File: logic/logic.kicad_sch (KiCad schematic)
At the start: 22 parts, among them J1 DIN41612_02x32_AC, U1 TPIC6595, U2 TPIC6595, U3 TPIC6595, U4 TPIC6595, U5 TPIC6595, U6 TPIC6595, U7 TPIC6595, U8 TPIC6595, U9 74HC14

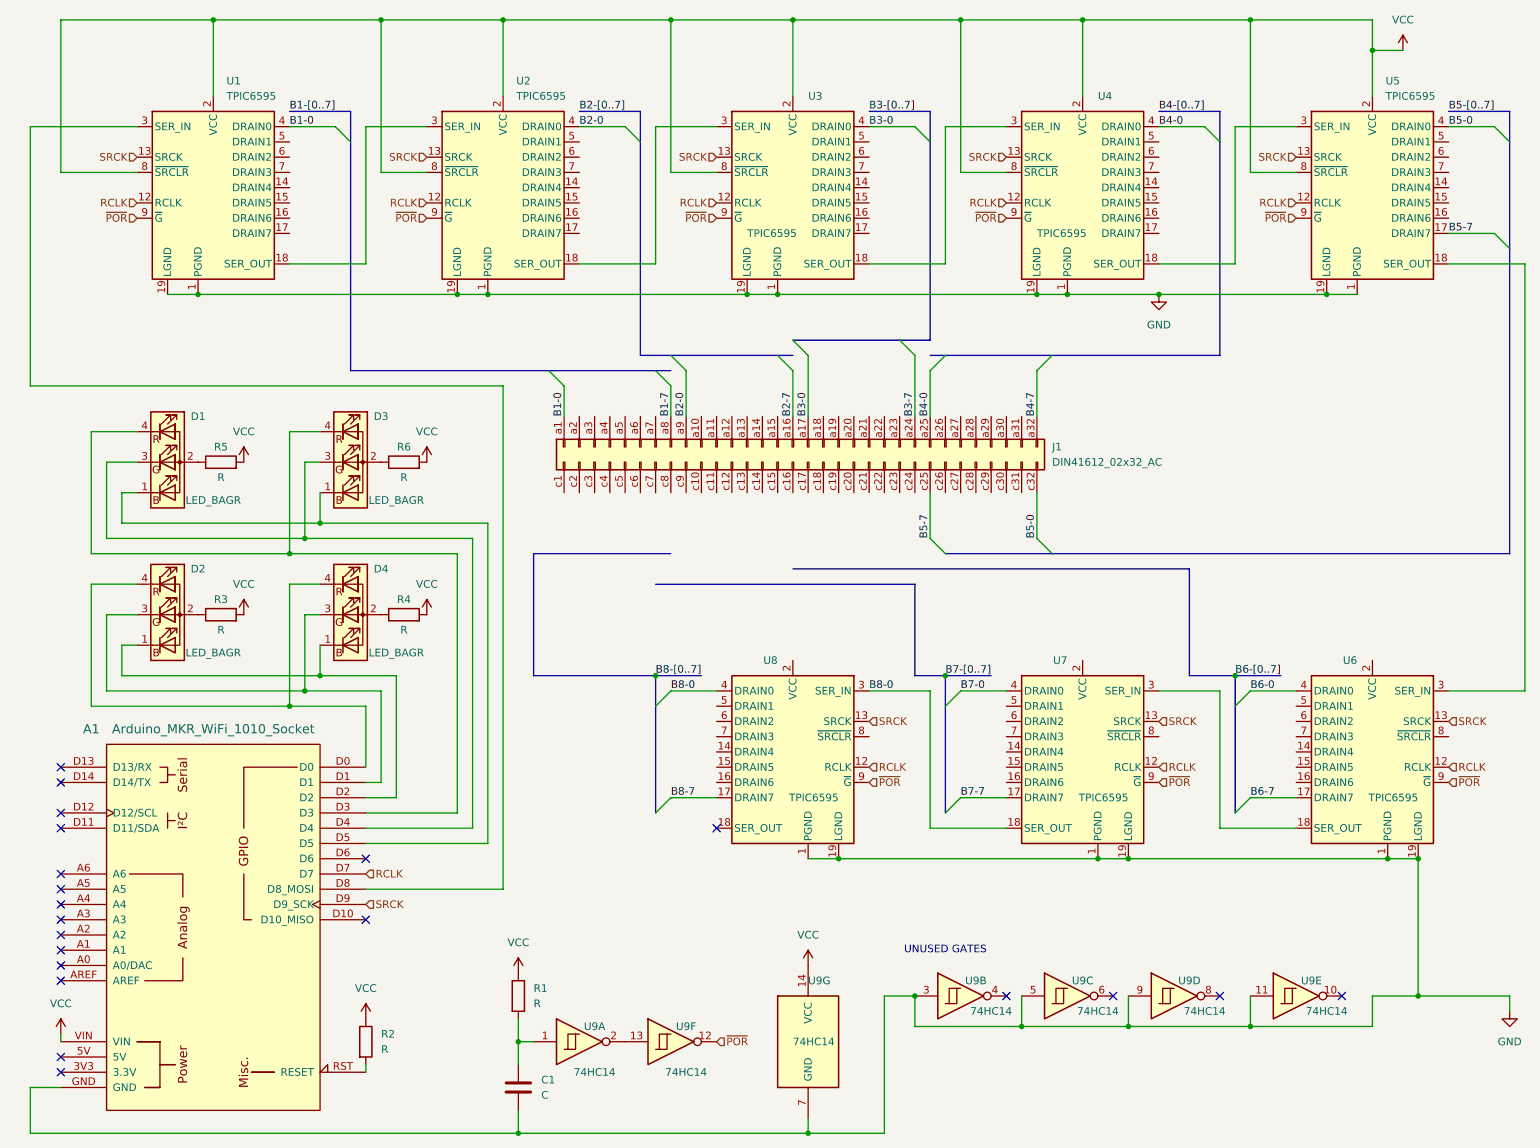
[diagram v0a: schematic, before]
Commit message: Commit obsolete version before major revision
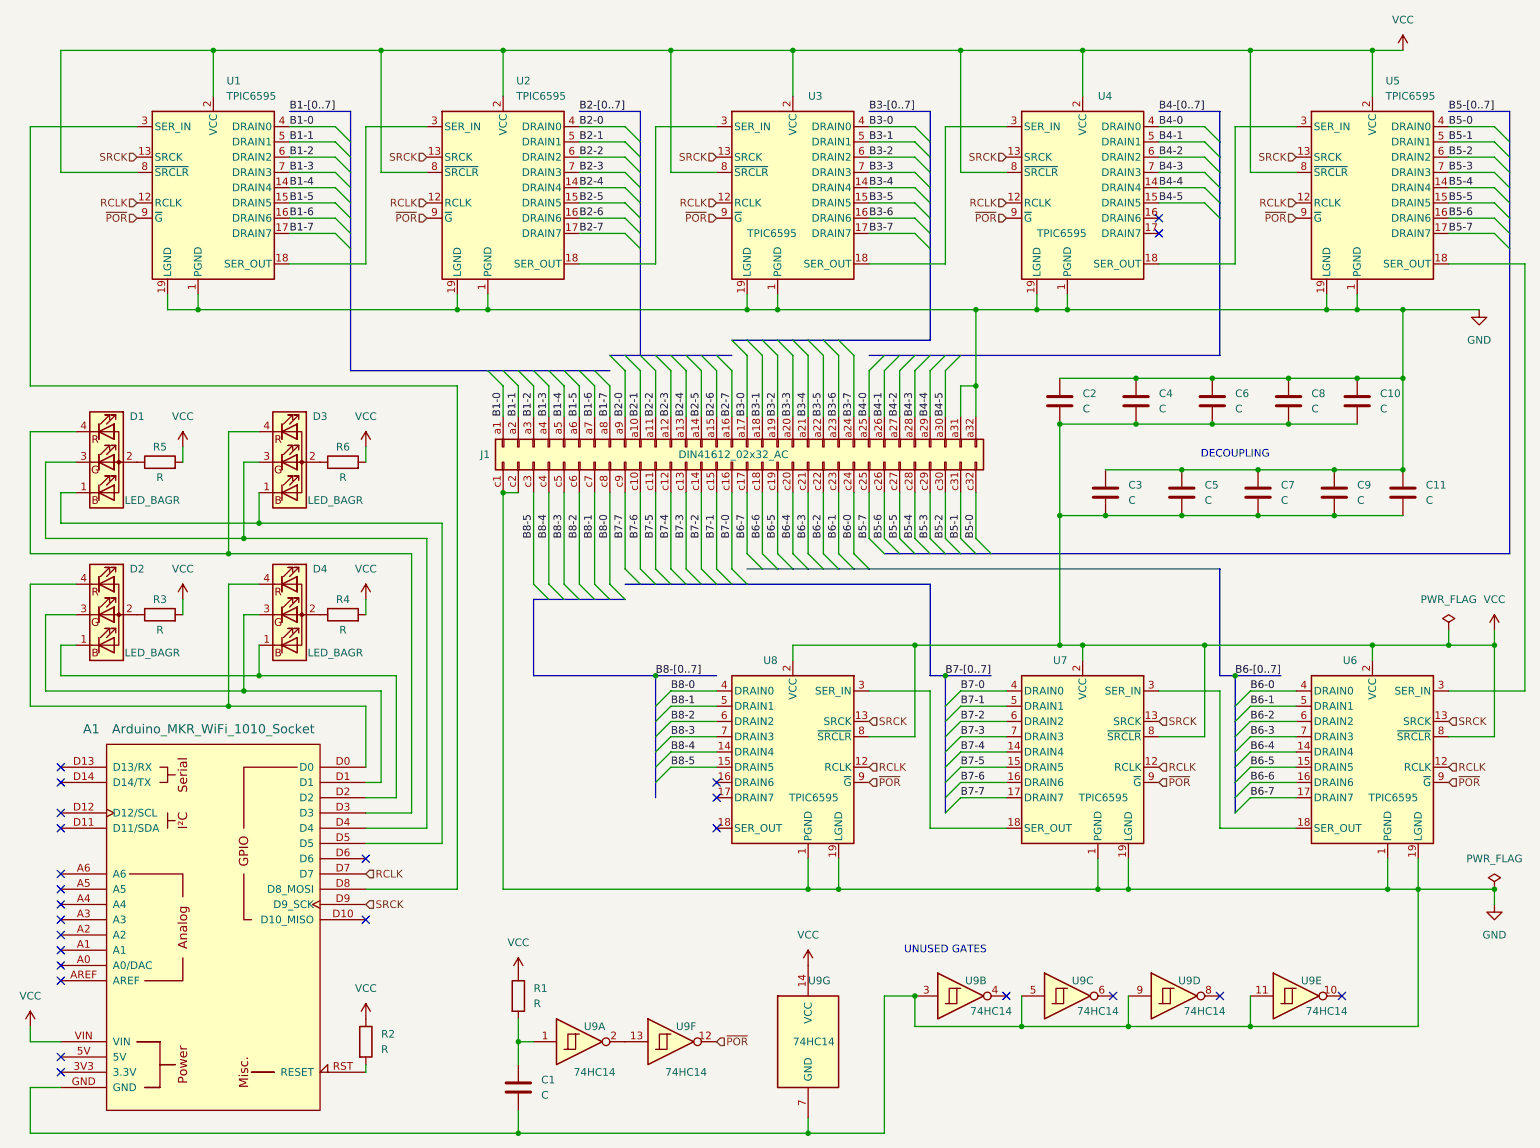
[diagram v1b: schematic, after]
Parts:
- added C10, C11, C2, C3, C4, C5, C6, C7, C8, C9: C, symbol Device:C
- J1: footprint (none) -> Connector_DIN:DIN41612_R_2x32_Male_Vertical_THT
- U1: footprint (none) -> Package_DIP:DIP-20_W7.62mm_Socket
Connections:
- net B4-7 is gone; now on net GND: J1.a32 (Pin_a32)
- net B1-7: now also U1.17 (DRAIN7)
- net B2-7: now also U2.17 (DRAIN7)
- net B3-7: now also U3.17 (DRAIN7)
- net B6-0: now also J1.c24 (Pin_c24)
- net B6-7: now also J1.c17 (Pin_c17)
- net B7-0: now also J1.c16 (Pin_c16)
- net B7-7: now also J1.c9 (Pin_c9)
- net B8-0: now also J1.c8 (Pin_c8); no longer U7.18 (SER_OUT), U8.3 (SER_IN)
- net GND: now also J1.a31 (Pin_a31), J1.c1 (Pin_c1), J1.c2 (Pin_c2), C10.1, C11.1, C2.1, C3.1, C4.1, C5.1, C6.1, C7.1, C8.1, C9.1
- net VCC: now also U6.2 (VCC), U6.8 (~{SRCLR}), U7.2 (VCC), U7.8 (~{SRCLR}), U8.2 (VCC), U8.8 (~{SRCLR}), C10.2, C11.2, C2.2, C3.2, C4.2, C5.2, C6.2, C7.2, C8.2, C9.2
- net B3-4: now reaches U3.14 (DRAIN4)
- net B3-4: now also J1.a21 (Pin_a21)
- net B3-5: now reaches U3.15 (DRAIN5)
- net B3-5: now also J1.a22 (Pin_a22)
- net B3-6: now reaches U3.16 (DRAIN6)
- net B3-6: now also J1.a23 (Pin_a23)
- net B3-1: now reaches U3.5 (DRAIN1)
- net B3-1: now also J1.a18 (Pin_a18)
- net B3-2: now reaches U3.6 (DRAIN2)
- net B3-2: now also J1.a19 (Pin_a19)
- net B3-3: now reaches U3.7 (DRAIN3)
- net B3-3: now also J1.a20 (Pin_a20)
- net B2-4: now reaches U2.14 (DRAIN4)
- net B2-4: now also J1.a13 (Pin_a13)
- net B2-5: now reaches U2.15 (DRAIN5)
- net B2-5: now also J1.a14 (Pin_a14)
- net B2-6: now reaches U2.16 (DRAIN6)
- net B2-6: now also J1.a15 (Pin_a15)
- net B2-1: now reaches U2.5 (DRAIN1)
- net B2-1: now also J1.a10 (Pin_a10)
- net B2-2: now reaches U2.6 (DRAIN2)
- net B2-2: now also J1.a11 (Pin_a11)
- net B2-3: now reaches U2.7 (DRAIN3)
- net B2-3: now also J1.a12 (Pin_a12)
- net B1-4: now reaches U1.14 (DRAIN4)
- net B1-4: now also J1.a5 (Pin_a5)
- net B1-5: now reaches U1.15 (DRAIN5)
- net B1-5: now also J1.a6 (Pin_a6)
- net B1-6: now reaches U1.16 (DRAIN6)
- net B1-6: now also J1.a7 (Pin_a7)
- net B1-1: now reaches U1.5 (DRAIN1)
- net B1-1: now also J1.a2 (Pin_a2)
- net B1-2: now reaches U1.6 (DRAIN2)
- net B1-2: now also J1.a3 (Pin_a3)
- net B1-3: now reaches U1.7 (DRAIN3)
- net B1-3: now also J1.a4 (Pin_a4)
- net B4-1: now reaches J1.a26 (Pin_a26)
- net B4-1: now also U4.5 (DRAIN1)
- net B4-2: now reaches J1.a27 (Pin_a27)
- net B4-2: now also U4.6 (DRAIN2)
- net B4-3: now reaches J1.a28 (Pin_a28)
- net B4-3: now also U4.7 (DRAIN3)
- net B4-4: now reaches J1.a29 (Pin_a29)
- net B4-4: now also U4.14 (DRAIN4)
- net B4-5: now reaches J1.a30 (Pin_a30)
- net B4-5: now also U4.15 (DRAIN5)
- net B7-6: now reaches J1.c10 (Pin_c10)
- net B7-6: now also U7.16 (DRAIN6)
- net B7-5: now reaches J1.c11 (Pin_c11)
- net B7-5: now also U7.15 (DRAIN5)
- net B7-4: now reaches J1.c12 (Pin_c12)
- net B7-4: now also U7.14 (DRAIN4)
- net B7-3: now reaches J1.c13 (Pin_c13)
- net B7-3: now also U7.7 (DRAIN3)
- net B7-2: now reaches J1.c14 (Pin_c14)
- net B7-2: now also U7.6 (DRAIN2)
- net B7-1: now reaches J1.c15 (Pin_c15)
- net B7-1: now also U7.5 (DRAIN1)
- net B6-6: now reaches J1.c18 (Pin_c18)
- net B6-6: now also U6.16 (DRAIN6)
- net B6-5: now reaches J1.c19 (Pin_c19)
- net B6-5: now also U6.15 (DRAIN5)
- net B6-4: now reaches J1.c20 (Pin_c20)
- net B6-4: now also U6.14 (DRAIN4)
- net B6-3: now reaches J1.c21 (Pin_c21)
- net B6-3: now also U6.7 (DRAIN3)
- net B6-2: now reaches J1.c22 (Pin_c22)
- net B6-2: now also U6.6 (DRAIN2)
- net B6-1: now reaches J1.c23 (Pin_c23)
- net B6-1: now also U6.5 (DRAIN1)
- net B5-6: now reaches J1.c26 (Pin_c26)
- net B5-6: now also U5.16 (DRAIN6)
- net B5-5: now reaches J1.c27 (Pin_c27)
- net B5-5: now also U5.15 (DRAIN5)
- net B5-4: now reaches J1.c28 (Pin_c28)
- net B5-4: now also U5.14 (DRAIN4)
- net B5-3: now reaches J1.c29 (Pin_c29)
- net B5-3: now also U5.7 (DRAIN3)
- net B8-5: now reaches J1.c3 (Pin_c3)
- net B8-5: now also U8.15 (DRAIN5)
- net B5-2: now reaches J1.c30 (Pin_c30)
- net B5-2: now also U5.6 (DRAIN2)
- net B5-1: now reaches J1.c31 (Pin_c31)
- net B5-1: now also U5.5 (DRAIN1)
- net B8-4: now reaches J1.c4 (Pin_c4)
- net B8-4: now also U8.14 (DRAIN4)
- net B8-3: now reaches J1.c5 (Pin_c5)
- net B8-3: now also U8.7 (DRAIN3)
- net B8-2: now reaches J1.c6 (Pin_c6)
- net B8-2: now also U8.6 (DRAIN2)
- net B8-1: now reaches J1.c7 (Pin_c7)
- net B8-1: now also U8.5 (DRAIN1)
- net B8-7: no longer names the net of U8.17 (DRAIN7)
- new net: U7.18 (SER_OUT), U8.3 (SER_IN)
- no-connect marks 21 -> 25
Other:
- note added: "DECOUPLING"
- moved on the sheet: D1, D2, D3, D4, J1, R3, R4, R5, R6

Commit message: Change to new 96-pin DIN-41612 schematic symbol in custom library
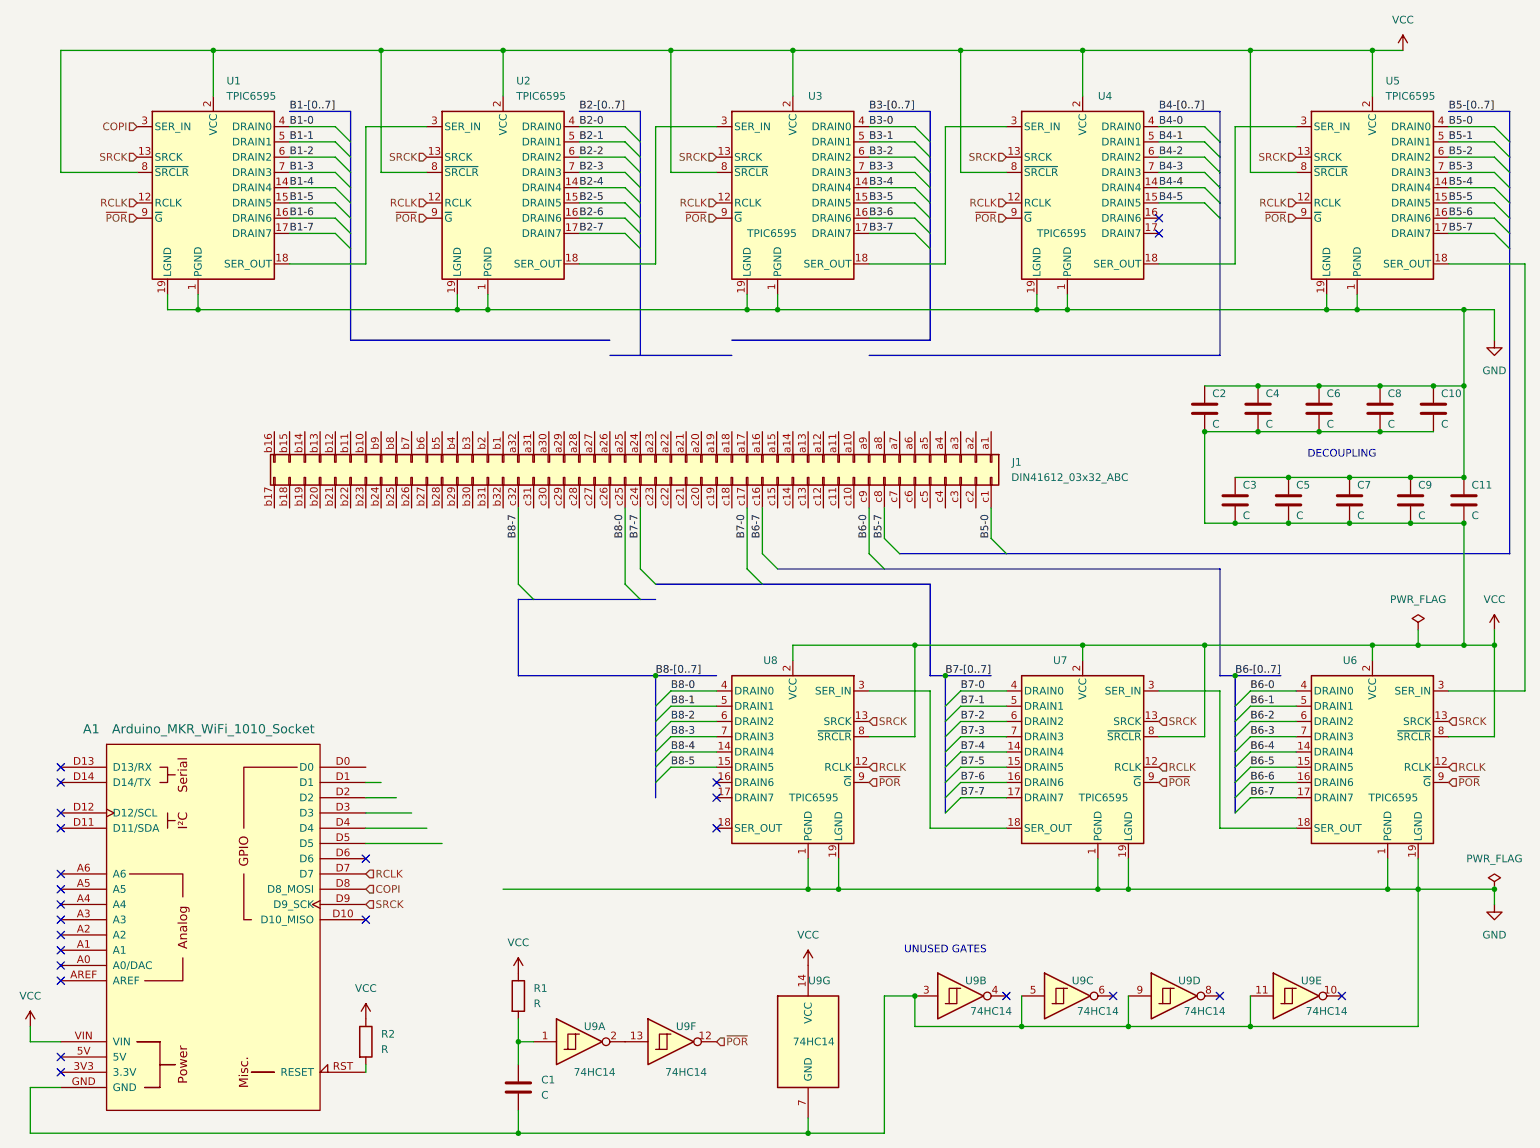
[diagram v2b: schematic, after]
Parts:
- removed D1, D2, D3, D4: LED_BAGR, symbol Device:LED_BAGR
- removed J1: DIN41612_02x32_AC, Connector_DIN:DIN41612_R_2x32_Male_Vertical_THT, symbol Connector:DIN41612_02x32_AC
- removed R3, R4, R5, R6: R, symbol Device:R
- added J1: DIN41612_03x32_ABC, symbol NixComp:DIN41612_03x32_ABC
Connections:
- net B5-0: now also J1.c1 (Pin_c1)
- net B5-7: now also J1.c8 (Pin_c8)
- net B6-0: now also J1.c9 (Pin_c9)
- net B6-7: now also J1.c16 (Pin_c16)
- net B7-0: now also J1.c17 (Pin_c17)
- net B7-7: now also J1.c24 (Pin_c24)
- net B8-0: now also J1.c25 (Pin_c25)
- net COPI: now reaches A1.D8 (D8_MOSI), U1.3 (SER_IN)
- new net B8-7: J1.c32 (Pin_c32)
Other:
- moved on the sheet: C10, C11, C2, C3, C4, C5, C6, C7, C8, C9
